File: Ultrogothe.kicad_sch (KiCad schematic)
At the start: 3 parts, among them J1 Conn_01x20, J2 Conn_01x20, J5 Conn_02x07_Odd_Even

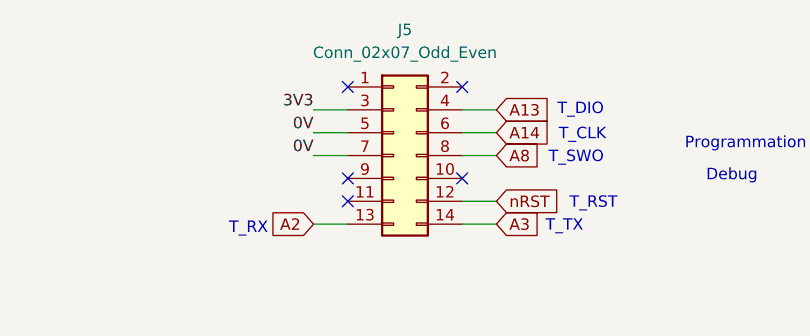
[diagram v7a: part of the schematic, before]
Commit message: chgt ST14 en CMS et fabrication
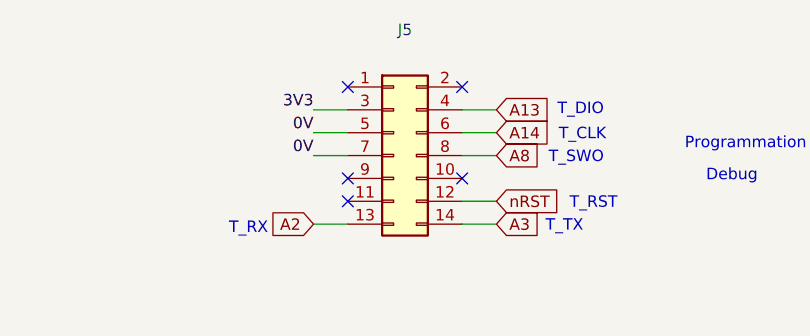
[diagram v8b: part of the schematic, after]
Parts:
- J1, J2: now left out of the parts list
- J5: footprint Connector_PinHeader_1.27mm:PinHeader_2x07_P1.27mm_Vertical -> Connector_PinHeader_1.27mm:PinHeader_2x07_P1.27mm_Vertical_SMD; LCSC (none) -> C3975190
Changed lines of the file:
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@@
 		(unit 1)
 		(exclude_from_sim no)
-		(in_bom yes)
+		(in_bom no)
 		(on_board yes)
 		(dnp no)
@@
 		(unit 1)
 		(exclude_from_sim no)
-		(in_bom yes)
+		(in_bom no)
 		(on_board yes)
 		(dnp no)
@@
 					(size 1.27 1.27)
 				)
-			)
-		)
-		(property "Footprint" "Connector_PinHeader_1.27mm:PinHeader_2x07_P1.27mm_Vertical"
+				(hide yes)
+			)
+		)
+		(property "Footprint" "Connector_PinHeader_1.27mm:PinHeader_2x07_P1.27mm_Vertical_SMD"
 			(at 224.79 52.07 0)
 			(effects
@@
 			(at 224.79 52.07 0)
 			(effects
+				(font
+					(size 1.27 1.27)
+				)
+				(hide yes)
+			)
+		)
+		(property "LCSC" "C3975190"
+			(at 224.79 52.07 0)
+			(effects
